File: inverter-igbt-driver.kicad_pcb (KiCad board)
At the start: 2 copper layers, 77 parts, among them J1 Conn_01x06, J2 Conn_01x06, U1 NE555, U2 IXDF604SIA, U3 FOD8316, U4 NE555, U5 FOD8316, U6 Transformer_2P_2S, U7 IXDF604SIA, U8 Transformer_2P_2S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

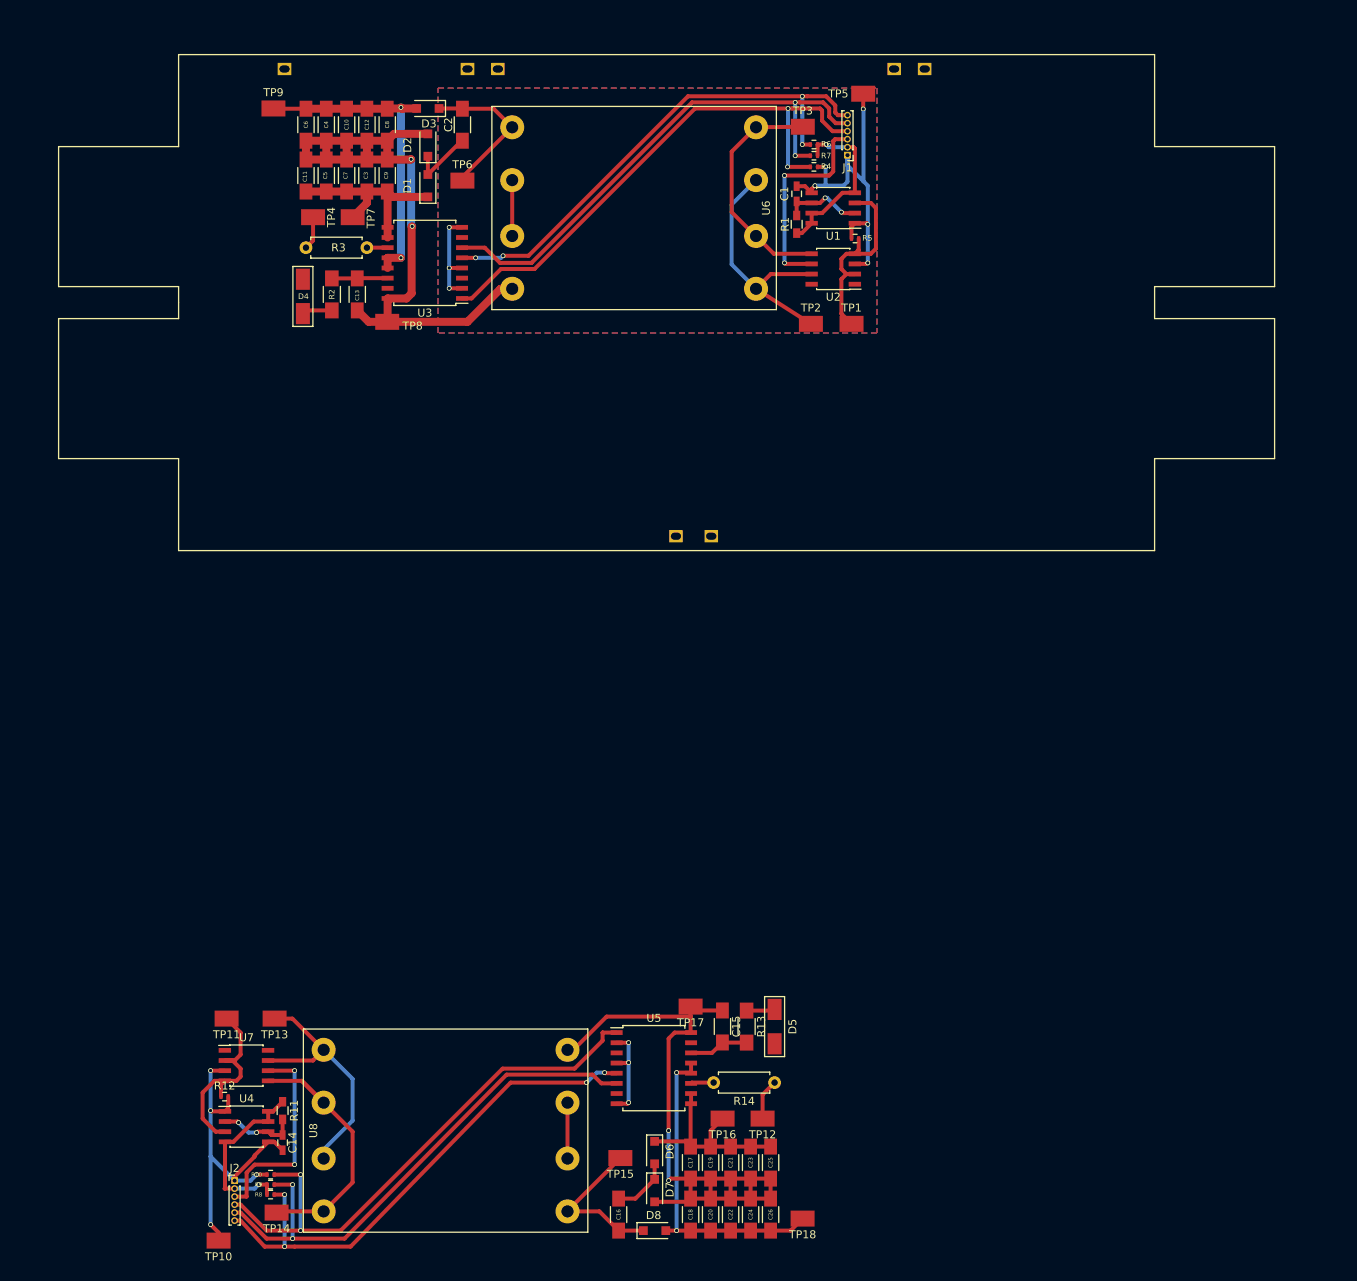
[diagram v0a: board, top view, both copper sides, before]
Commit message: Move square wave generator to single module.
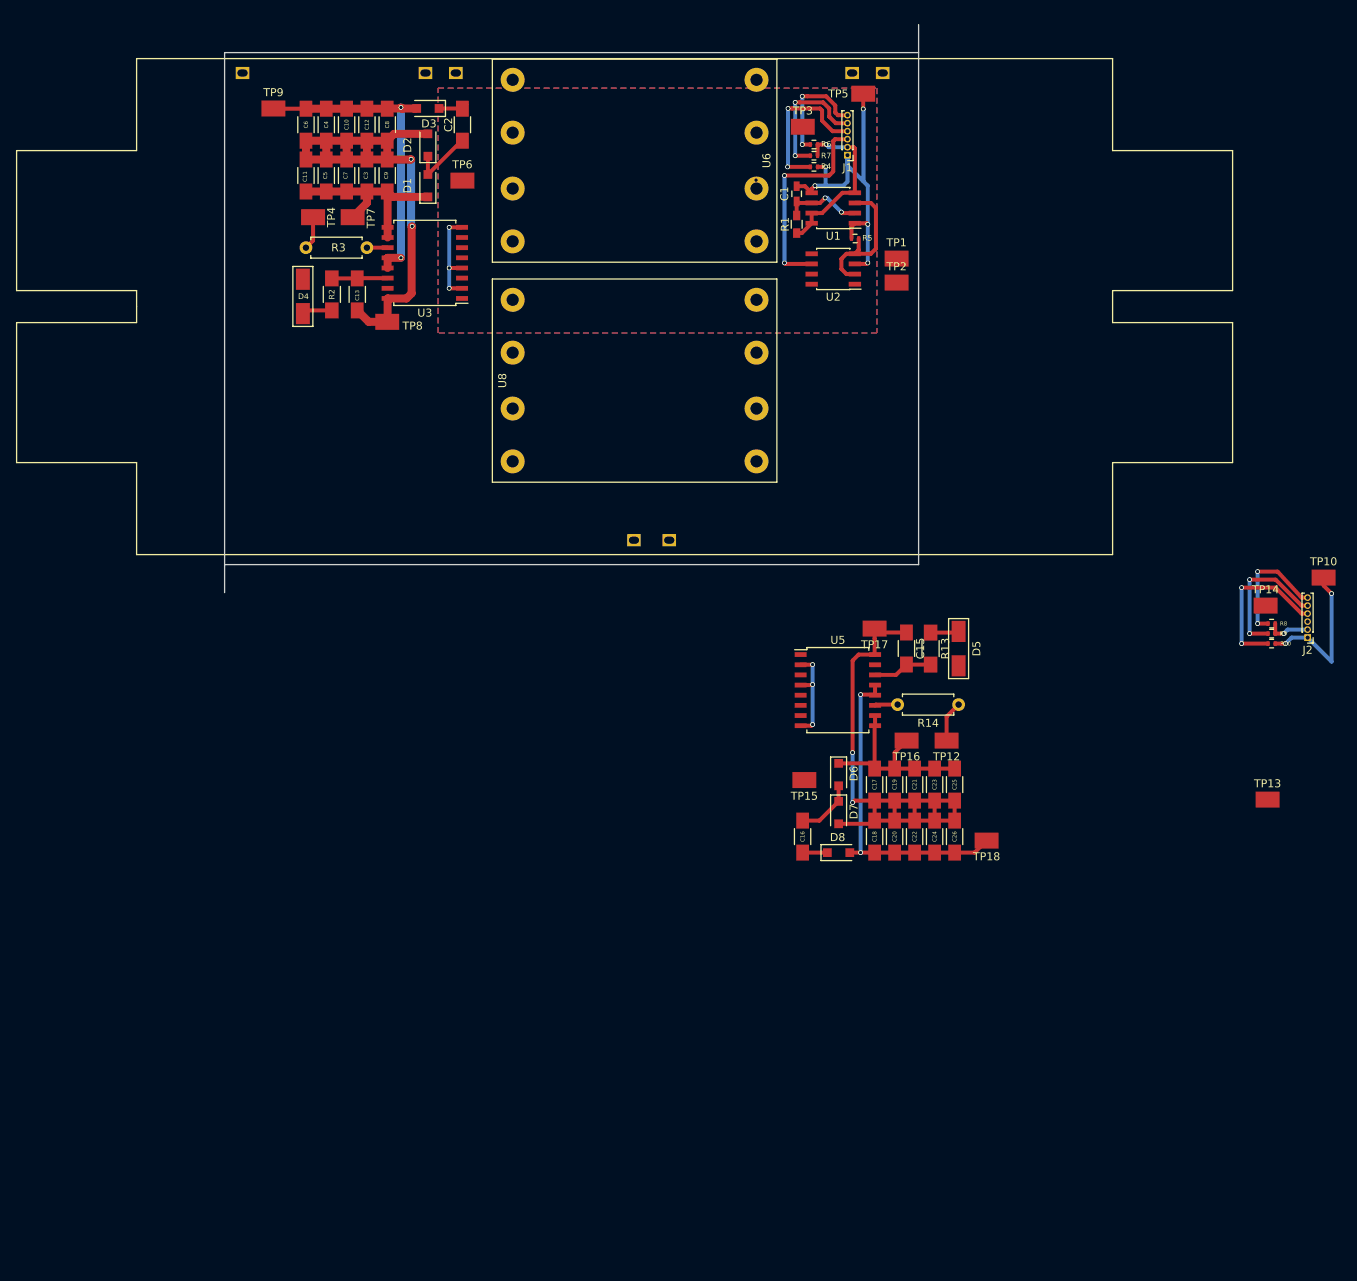
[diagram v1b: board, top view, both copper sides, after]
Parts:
- removed C14: 0.01u, Capacitors_SMD:C_0603_HandSoldering
- removed R11: 1.5k, Resistors_SMD:R_0603_HandSoldering
- removed R12: 1k, Resistors_SMD:R_0402
- removed TP11: TEST, inverter-igbt-driver:TP RCT (0805)
- removed U4: NE555, Housings_SOIC:SOIC-8_3.9x4.9mm_Pitch1.27mm
- removed U7: IXDF604SIA, Housings_SOIC:SOIC-8_3.9x4.9mm_Pitch1.27mm
- moved TP10 161.1 mm to (230.1, 86.6), turned to 180 degrees
- moved J2 150.3 mm to (228.1, 94.1), turned to 180 degrees
- moved TP14 145.1 mm to (222.9, 90.1), turned to 180 degrees
- moved R8 144.1 mm to (223.6, 92.4), turned to 180 degrees
- moved R9 142.8 mm to (223.6, 93.6), turned to 180 degrees
- moved R10 141.6 mm to (223.6, 94.9), turned to 0 degrees
- moved TP13 127.1 mm to (223.1, 114.4), turned to 180 degrees
- moved U8 96.7 mm to (144.0, 62.0)
- moved C15 52.6 mm to (178.0, 95.5)
- moved U5 52.6 mm to (169.4, 100.7)
- moved C16 52.6 mm to (165.0, 119.0)
- moved C17 52.6 mm to (174.0, 112.5)
- moved C18 52.6 mm to (174.0, 119.0)
- moved C19 52.6 mm to (176.5, 112.5)
- moved C20 52.6 mm to (176.5, 119.0)
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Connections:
- TP13 pad 1: Net-(TP13-Pad1) -> /negative/SQUARE_H
- TP14 pad 1: Net-(TP14-Pad1) -> /negative/SQUARE_L
- TP2 pad 1: Net-(TP2-Pad1) -> /negative/SQUARE_H
- TP3 pad 1: Net-(TP3-Pad1) -> /positive/SQUARE_L
- U2 pad 5: Net-(TP3-Pad1) -> /negative/SQUARE_L
- U2 pad 7: Net-(TP2-Pad1) -> /negative/SQUARE_H
- U6 pad 1: Net-(TP2-Pad1) -> /negative/SQUARE_H
- U6 pad 2: Net-(TP3-Pad1) -> /positive/SQUARE_L
- U6 pad 3: Net-(TP2-Pad1) -> /negative/SQUARE_H
- U6 pad 4: Net-(TP3-Pad1) -> /positive/SQUARE_L
- U8 pad 1: Net-(TP13-Pad1) -> /negative/SQUARE_H
- U8 pad 2: Net-(TP14-Pad1) -> /negative/SQUARE_L
- U8 pad 3: Net-(TP13-Pad1) -> /negative/SQUARE_H
- U8 pad 4: Net-(TP14-Pad1) -> /negative/SQUARE_L
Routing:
- net /RESET_H: track 65.1 -> 14.2 mm, vias 4 -> 2
- net /FAULT_H: track 67.5 -> 16.8 mm
- net /RESET_L: track 66.2 -> 15.5 mm, vias 4 -> 2
- net /VIN_H: track 70.1 -> 19.5 mm
- net /VIN_L: track 70.2 -> 19.9 mm
- net /FAULT_L: track 67.2 -> 17.6 mm
- net Net-(TP14-Pad1): track 34.0 -> 0.00 mm
- net Net-(TP2-Pad1): track 32.0 -> 0.00 mm, vias 1 -> 0
- net Net-(TP13-Pad1): track 31.8 -> 0.00 mm
- net Net-(TP3-Pad1): track 29.9 -> 0.00 mm
- net +24V: track 52.3 -> 26.4 mm, vias 4 -> 2
- net Net-(R12-Pad1): track 25.4 -> 0.00 mm
- net GND: track 114.3 -> 89.1 mm, vias 15 -> 13
- net /COLL_L: track 85.2 -> 67.9 mm
- net +5V: track 44.6 -> 27.4 mm
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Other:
- board outline added: 86.8 x 71 mm

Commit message: Fixing layout
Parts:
- removed TP10, TP13, TP14: TEST, inverter-igbt-driver:TP RCT (0805)
- moved TP18 108.3 mm to (100.2, 56.0), turned to 180 degrees
- moved D5 100.9 mm to (94.8, 49.5), turned to 270 degrees
- moved C26 100.4 mm to (104.1, 58.1), turned to 90 degrees
- moved C24 96.5 mm to (106.6, 58.1), turned to 90 degrees
- moved R13 94.4 mm to (94.8, 57.2)
- moved C25 93.1 mm to (104.1, 64.6), turned to 90 degrees
- moved C22 92.7 mm to (109.1, 58.1), turned to 90 degrees
- moved TP12 90.6 mm to (100.2, 70.0), turned to 180 degrees
- moved C20 89.0 mm to (111.6, 58.1), turned to 90 degrees
- moved C23 88.9 mm to (106.6, 64.6), turned to 90 degrees
- moved TP16 87.7 mm to (100.2, 66.5), turned to 180 degrees
- moved R14 87.3 mm to (103.5, 70.0), turned to 0 degrees
- moved C18 85.4 mm to (114.1, 58.1), turned to 90 degrees
- moved C21 84.7 mm to (109.1, 64.6), turned to 90 degrees
- moved D8 82.4 mm to (118.6, 56.1), turned to 180 degrees
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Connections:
- TP3 pad 1: /positive/SQUARE_L -> /negative/SQUARE_L
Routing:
- net /EMIT_L: track 68.3 -> 121.2 mm, vias 2 -> 0
- net /GATE_L: track 5.12 -> 55.4 mm
- net Net-(C2-Pad2): track 4.14 -> 46.4 mm
- net /COLL_L: track 67.9 -> 107.4 mm, vias 2 -> 0
- net /negative/SQUARE_H: track 0.06 -> 32.9 mm
- net Net-(C15-Pad2): track 7.47 -> 32.4 mm, vias 0 -> 2
- net /GATE_H: track 4.18 -> 28.0 mm
- net /negative/SQUARE_L: track 0.09 -> 16.7 mm
- net /positive/SQUARE_L: track 0.00 -> 16.1 mm
- net GND: track 89.1 -> 74.0 mm, vias 13 -> 12
- net /positive/VDD_IGBT: track 39.9 -> 28.3 mm, vias 2 -> 0
- net Net-(C16-Pad2): track 3.10 -> 13.0 mm
- net Net-(U8-Pad6): track 0.00 -> 6.99 mm
- net Net-(U6-Pad6): track 0.00 -> 6.98 mm
- net Net-(D4-Pad2): track 3.79 -> 7.89 mm
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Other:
- board size 86.8 x 71 mm -> 87 x 64 mm

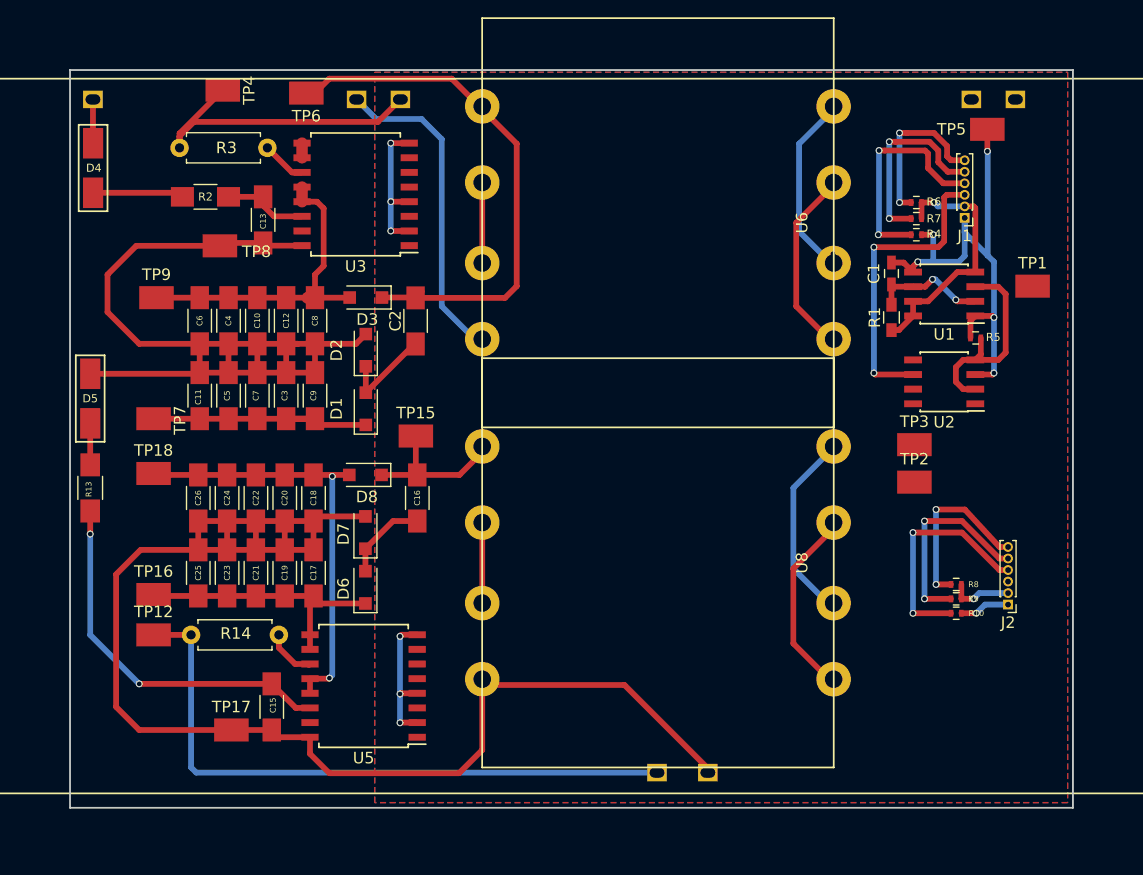
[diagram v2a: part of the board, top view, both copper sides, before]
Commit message: Completed layout with one connector.
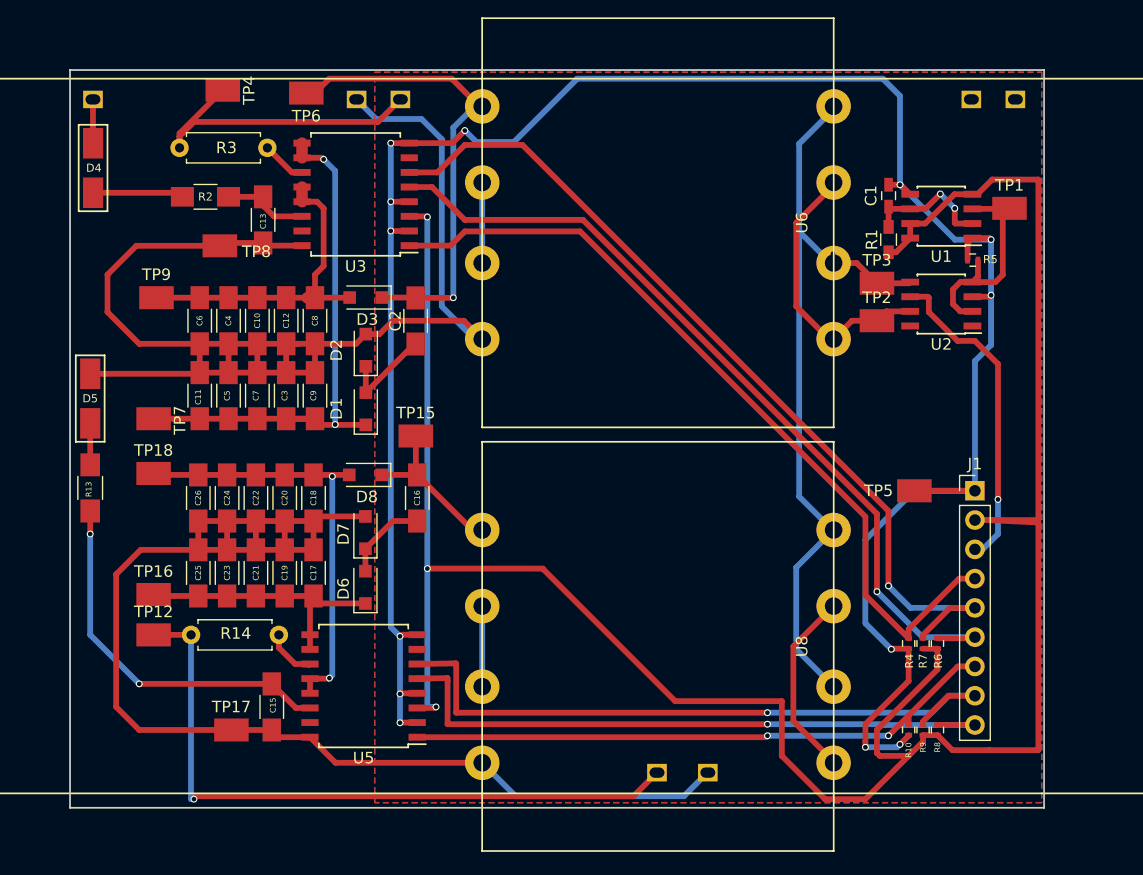
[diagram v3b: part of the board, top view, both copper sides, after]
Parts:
- removed J2: Conn_01x06, Pin_Headers:Pin_Header_Straight_1x06_Pitch1.00mm
- J1: value Conn_01x06 -> Conn_01x09; footprint Pin_Headers:Pin_Header_Straight_1x06_Pitch1.00mm -> Pin_Headers:Pin_Header_Straight_1x09_Pitch2.54mm
- moved R6 38.3 mm to (168.2, 70.8), turned to 90 degrees
- moved R7 36.9 mm to (167.0, 70.8), turned to 90 degrees
- moved R4 35.5 mm to (165.8, 70.8), turned to 270 degrees
- moved TP5 32.0 mm to (166.2, 57.5)
- moved J1 23.7 mm to (171.5, 57.5), turned to 0 degrees
- moved TP2 14.4 mm to (163.0, 42.8)
- moved TP3 14.4 mm to (163.0, 39.5)
- moved R8 12.7 mm to (168.2, 78.2), turned to 90 degrees
- moved R9 11.7 mm to (167.0, 78.2), turned to 90 degrees
- moved R10 10.9 mm to (165.8, 78.2), turned to 270 degrees
- moved U8 7.25 mm to (144.0, 71.0)
- moved TP1 7.04 mm to (174.5, 33.0)
- moved C1 6.75 mm to (164.0, 31.9)
- moved R1 6.75 mm to (164.0, 35.7)
- moved R5 6.75 mm to (171.3, 37.5)
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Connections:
- U6 pad 2: /positive/SQUARE_L -> /negative/SQUARE_L
- U6 pad 4: /positive/SQUARE_L -> /negative/SQUARE_L
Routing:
- net +5V: track 27.4 -> 205.7 mm, vias 2 -> 3
- net GND: track 74.0 -> 196.7 mm, vias 12 -> 13
- net /FAULT_H: track 16.8 -> 76.3 mm, vias 2 -> 1
- net /RESET_H: track 14.2 -> 72.5 mm, vias 2 -> 1
- net /VIN_H: track 19.5 -> 70.8 mm, vias 2 -> 0
- net /negative/SQUARE_L: track 16.7 -> 67.1 mm, vias 0 -> 1
- net /FAULT_L: track 17.6 -> 59.0 mm, vias 2 -> 1
- net /RESET_L: track 15.5 -> 55.7 mm, vias 2 -> 1
- net /VIN_L: track 19.9 -> 51.7 mm
- net /positive/VSS_IGBT: track 22.4 -> 47.8 mm, vias 0 -> 2
- net /positive/SQUARE_L: track 16.1 -> 0.00 mm, vias 1 -> 0
- net /COLL_L: track 107.4 -> 118.7 mm
- net /EMIT_L: track 121.2 -> 112.5 mm
- net /negative/SQUARE_H: track 32.9 -> 40.5 mm
- net Net-(C2-Pad2): track 46.4 -> 41.9 mm, vias 0 -> 1
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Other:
- board size 87 x 64 mm -> 84.5 x 64 mm

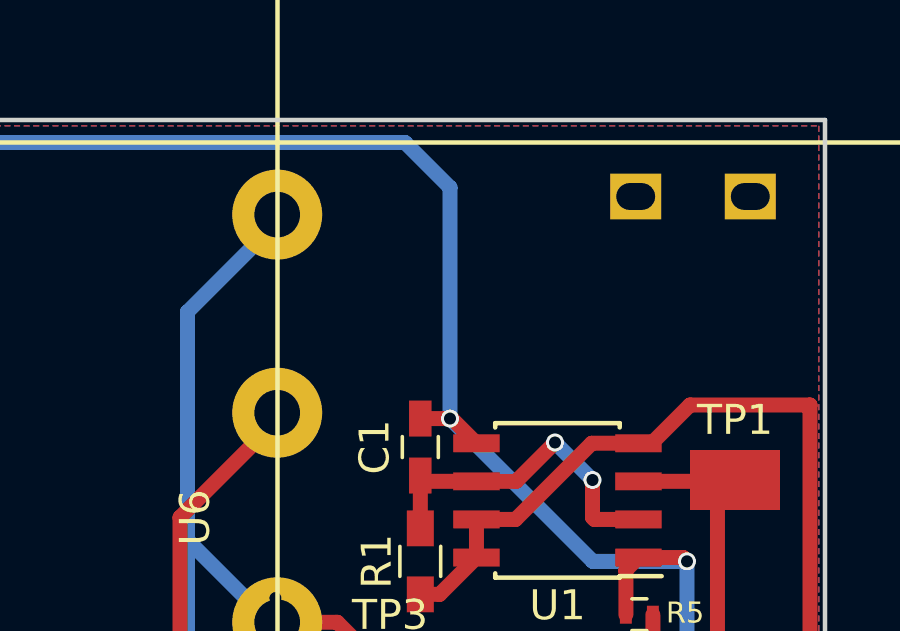
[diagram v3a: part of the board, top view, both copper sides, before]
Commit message: Changed 555 timer configuration.
555 timer was not behaving correctly. Added resistor to out for timing and increased resistor to 5V to mostly open circuit (in steady state).

Added extra coupling capacitor for control voltage.
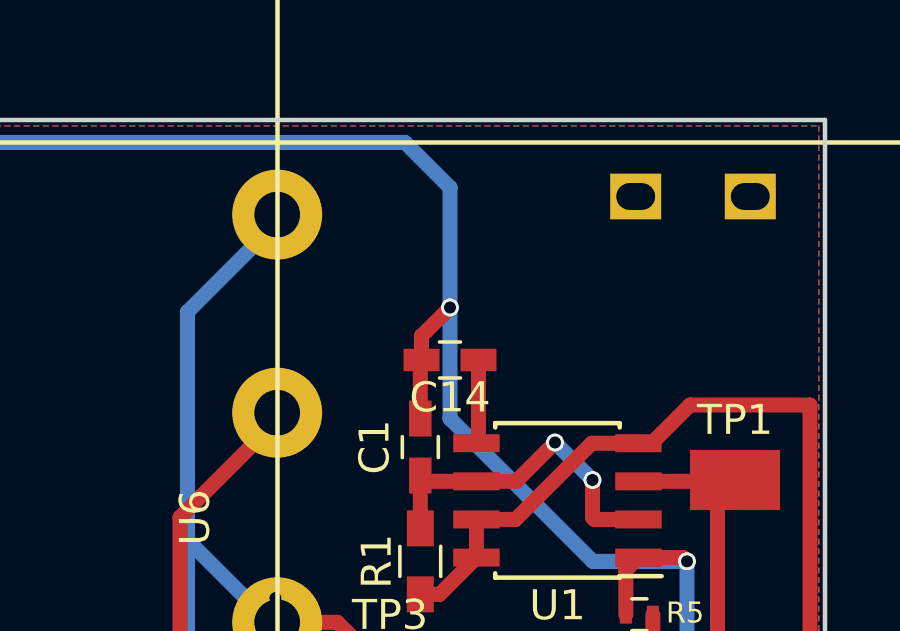
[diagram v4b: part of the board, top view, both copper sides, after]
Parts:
- added C14: 0.01u, Capacitors_SMD:C_0603_HandSoldering, F.Cu at (165.0, 29.0)
- R1: value 1.5k -> 100k
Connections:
- U1 pad 5: GND -> Net-(C14-Pad1)
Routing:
- net Net-(C14-Pad1): track 0.00 -> 2.80 mm
- net GND: track 196.7 -> 198.6 mm
